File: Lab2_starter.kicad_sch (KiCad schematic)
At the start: 76 parts, among them J1 973582101, J10 Conn_01x02, J11 Conn_01x02, J12 Conn_01x02, J13 Conn_01x02, J14 Conn_01x02, J15 Conn_01x02, J16 Conn_01x02, J2 973582100, J3 973582101, J4 973582100, J5 Conn_01x01, J6 Conn_01x01, J7 Conn_01x02, J8 Conn_01x02, J9 Conn_01x02, Q1 NMOS, Q2 NMOS, SW1 SW_Push_DPDT, U1 IR2010, U2 CT416-HSN820DR, U3 LAUNCHXL-F28P55X_BottomHalf

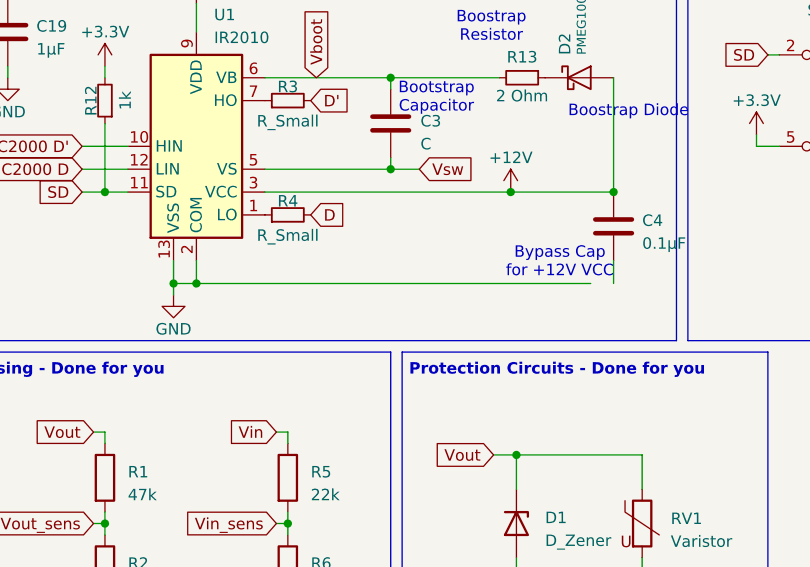
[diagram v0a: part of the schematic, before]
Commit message: Creating gating loop
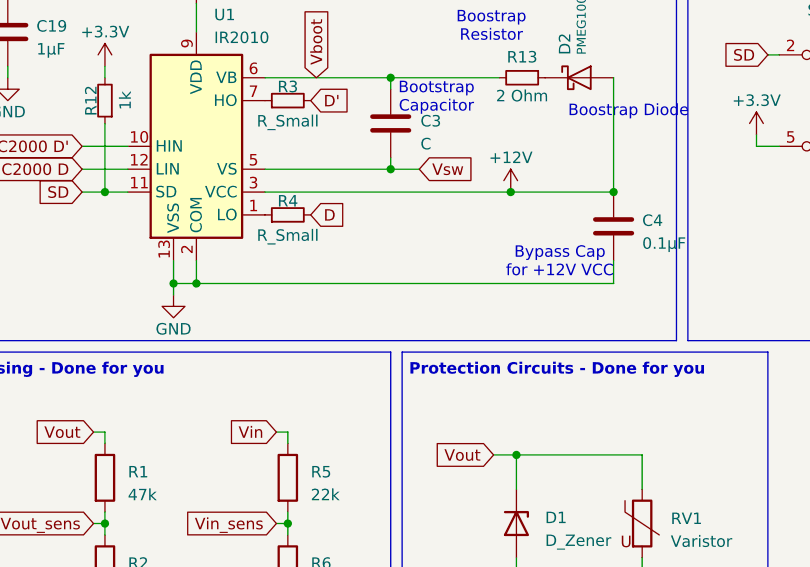
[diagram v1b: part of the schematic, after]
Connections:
- net GND: now also C4.2
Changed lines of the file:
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@@
 	(wire
 		(pts
-			(xy 41.91 120.65) (xy 85.725 120.65)
+			(xy 41.91 120.65) (xy 88.265 120.65)
 		)
 		(stroke

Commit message: Everything
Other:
- moved on the sheet: D1, RV1
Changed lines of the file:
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@@
 	)
 	(junction
-		(at 77.47 139.7)
+		(at 78.105 139.7)
 		(diameter 0)
 		(color 0 0 0 0)
@@
 	)
 	(junction
-		(at 77.47 154.94)
+		(at 78.105 154.94)
 		(diameter 0)
 		(color 0 0 0 0)
@@
 	(wire
 		(pts
-			(xy 77.47 139.7) (xy 77.47 143.51)
+			(xy 78.105 139.7) (xy 78.105 143.51)
 		)
 		(stroke
@@
 	(wire
 		(pts
-			(xy 77.47 151.13) (xy 77.47 154.94)
+			(xy 78.105 151.13) (xy 78.105 154.94)
 		)
 		(stroke
@@
 	(wire
 		(pts
-			(xy 77.47 154.94) (xy 77.47 156.21)
+			(xy 78.105 154.94) (xy 78.105 156.21)
 		)
 		(stroke
@@
 	(wire
 		(pts
-			(xy 74.93 139.7) (xy 77.47 139.7)
+			(xy 75.565 139.7) (xy 78.105 139.7)
 		)
 		(stroke
@@
 	(wire
 		(pts
-			(xy 91.44 143.51) (xy 91.44 139.7)
+			(xy 92.075 143.51) (xy 92.075 139.7)
 		)
 		(stroke
@@
 	(wire
 		(pts
-			(xy 77.47 139.7) (xy 91.44 139.7)
+			(xy 78.105 139.7) (xy 92.075 139.7)
 		)
 		(stroke
@@
 	(wire
 		(pts
-			(xy 77.47 154.94) (xy 91.44 154.94)
+			(xy 78.105 154.94) (xy 92.075 154.94)
 		)
 		(stroke
@@
 	(wire
 		(pts
-			(xy 91.44 151.13) (xy 91.44 154.94)
+			(xy 92.075 151.13) (xy 92.075 154.94)
 		)
 		(stroke
@@
 	(global_label "C2000 D "
 		(shape input)
-		(at 29.21 107.95 180)
+		(at 29.21 107.95 0)
 		(fields_autoplaced yes)
 		(effects
@@
 				(size 1.27 1.27)
 			)
-			(justify right)
+			(justify left)
 		)
 		(property "Intersheetrefs" "${INTERSHEET_REFS}"
-			(at 17.9208 107.95 0)
+			(at 40.4992 107.95 0)
 			(effects
 				(font
 					(size 1.27 1.27)
 				)
-				(justify right)
+				(justify left)
 				(hide yes)
 			)
@@
 	(global_label "Vout"
 		(shape input)
-		(at 74.93 139.7 180)
+		(at 75.565 139.7 180)
 		(fields_autoplaced yes)
 		(effects
@@
 		)
 		(property "Intersheetrefs" "${INTERSHEET_REFS}"
-			(at 67.9119 139.7 0)
+			(at 68.5469 139.7 0)
 			(effects
 				(font
@@
 	(symbol
 		(lib_id "Device:D_Zener")
-		(at 77.47 147.32 270)
+		(at 78.105 147.32 270)
 		(unit 1)
 		(exclude_from_sim no)
@@
 		(fields_autoplaced yes)
 		(property "Reference" "D1"
-			(at 80.645 146.685 90)
+			(at 81.28 146.685 90)
 			(effects
 				(font
@@
 		)
 		(property "Value" "D_Zener"
-			(at 80.645 149.225 90)
+			(at 81.28 149.225 90)
 			(effects
 				(font
@@
 		)
 		(property "Footprint" "ECE462L:1.5KE75A"
-			(at 77.47 147.32 0)
+			(at 78.105 147.32 0)
 			(effects
 				(font
@@
 		)
 		(property "Datasheet" "~"
-			(at 77.47 147.32 0)
+			(at 78.105 147.32 0)
 			(effects
 				(font
@@
 		)
 		(property "Description" ""
-			(at 77.47 147.32 0)
+			(at 78.105 147.32 0)
 			(effects
 				(font
@@
 	(symbol
 		(lib_id "Device:Varistor")
-		(at 91.44 147.32 0)
+		(at 92.075 147.32 0)
 		(unit 1)
 		(exclude_from_sim no)
@@
 		(fields_autoplaced yes)
 		(property "Reference" "RV1"
-			(at 94.615 146.7842 0)
+			(at 95.25 146.7842 0)
 			(effects
 				(font
@@
 		)
 		(property "Value" "Varistor"
-			(at 94.615 149.3242 0)
+			(at 95.25 149.3242 0)
 			(effects
 				(font
@@
 		)
 		(property "Footprint" "ECE462L:V100ZA15P"
-			(at 89.662 147.32 90)
+			(at 90.297 147.32 90)
 			(effects
 				(font
@@
 		)
 		(property "Datasheet" "~"
-			(at 91.44 147.32 0)
+			(at 92.075 147.32 0)
 			(effects
 				(font
@@
 		)
 		(property "Description" ""
-			(at 91.44 147.32 0)
+			(at 92.075 147.32 0)
 			(effects
 				(font
@@
 		)
 		(property "Sim.Name" "kicad_builtin_varistor"
-			(at 91.44 147.32 0)
+			(at 92.075 147.32 0)
 			(effects
 				(font
@@
 		)
 		(property "Sim.Device" "SUBCKT"
-			(at 91.44 147.32 0)
+			(at 92.075 147.32 0)
 			(effects
 				(font
@@
 		)
 		(property "Sim.Pins" "1=A 2=B"
-			(at 91.44 147.32 0)
+			(at 92.075 147.32 0)
 			(effects
 				(font
@@
 		)
 		(property "Sim.Params" "threshold=1k"
-			(at 91.44 147.32 0)
+			(at 92.075 147.32 0)
 			(effects
 				(font
@@
 		)
 		(property "Sim.Library" "${KICAD7_SYMBOL_DIR}/Simulation_SPICE.sp"
-			(at 91.44 147.32 0)
+			(at 92.075 147.32 0)
 			(effects
 				(font
@@
 	(symbol
 		(lib_id "power:GND")
-		(at 77.47 156.21 0)
+		(at 78.105 156.21 0)
 		(unit 1)
 		(exclude_from_sim no)
@@
 		(dnp no)
 		(property "Reference" "#PWR01"
-			(at 77.47 162.56 0)
+			(at 78.105 162.56 0)
 			(effects
 				(font
@@
 		)
 		(property "Value" "GND"
-			(at 77.47 160.274 0)
+			(at 78.105 160.274 0)
 			(effects
 				(font
@@
 		)
 		(property "Footprint" ""
-			(at 77.47 156.21 0)
+			(at 78.105 156.21 0)
 			(effects
 				(font
@@
 		)
 		(property "Datasheet" ""
-			(at 77.47 156.21 0)
+			(at 78.105 156.21 0)
 			(effects
 				(font
@@
 		)
 		(property "Description" ""
-			(at 77.47 156.21 0)
+			(at 78.105 156.21 0)
 			(effects
 				(font

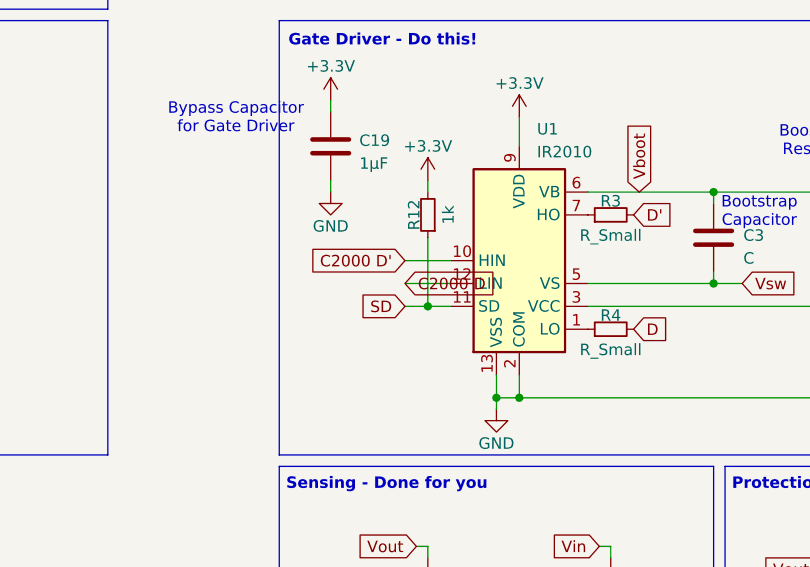
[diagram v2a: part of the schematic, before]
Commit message: Added planes and fixed for DRC
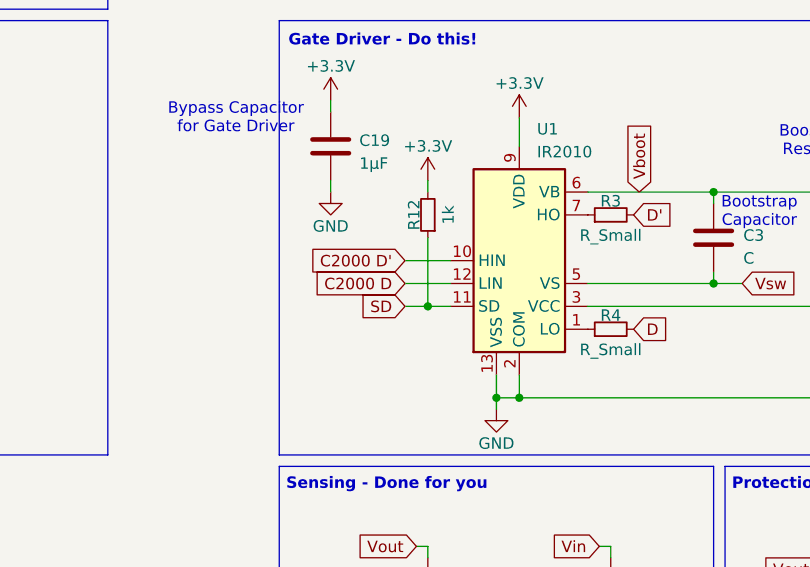
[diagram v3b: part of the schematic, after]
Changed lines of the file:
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@@
 	(global_label "C2000 D "
 		(shape input)
-		(at 29.21 107.95 0)
+		(at 29.21 107.95 180)
 		(fields_autoplaced yes)
 		(effects
@@
 				(size 1.27 1.27)
 			)
-			(justify left)
+			(justify right)
 		)
 		(property "Intersheetrefs" "${INTERSHEET_REFS}"
-			(at 40.4992 107.95 0)
+			(at 16.9116 107.95 0)
 			(effects
 				(font
 					(size 1.27 1.27)
 				)
-				(justify left)
+				(justify right)
 				(hide yes)
 			)
